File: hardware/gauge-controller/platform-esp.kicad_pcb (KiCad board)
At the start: 4 copper layers, 50 x 49.6 mm, 107 parts, among them J1 Conn_ARM_JTAG_SWD_10, J3 PWR_CAN, J4 USB4120-03-C_REVA, J6 TC2030-IDC, SW1 SW_Push, SW2 SW_Push, U1 W25Q128JVS, U2 ESP-PSRAM32, U3 ESP32-S3R2, U4 AP64200Q, U5 LTC2875-DD, Y1 40MHZ

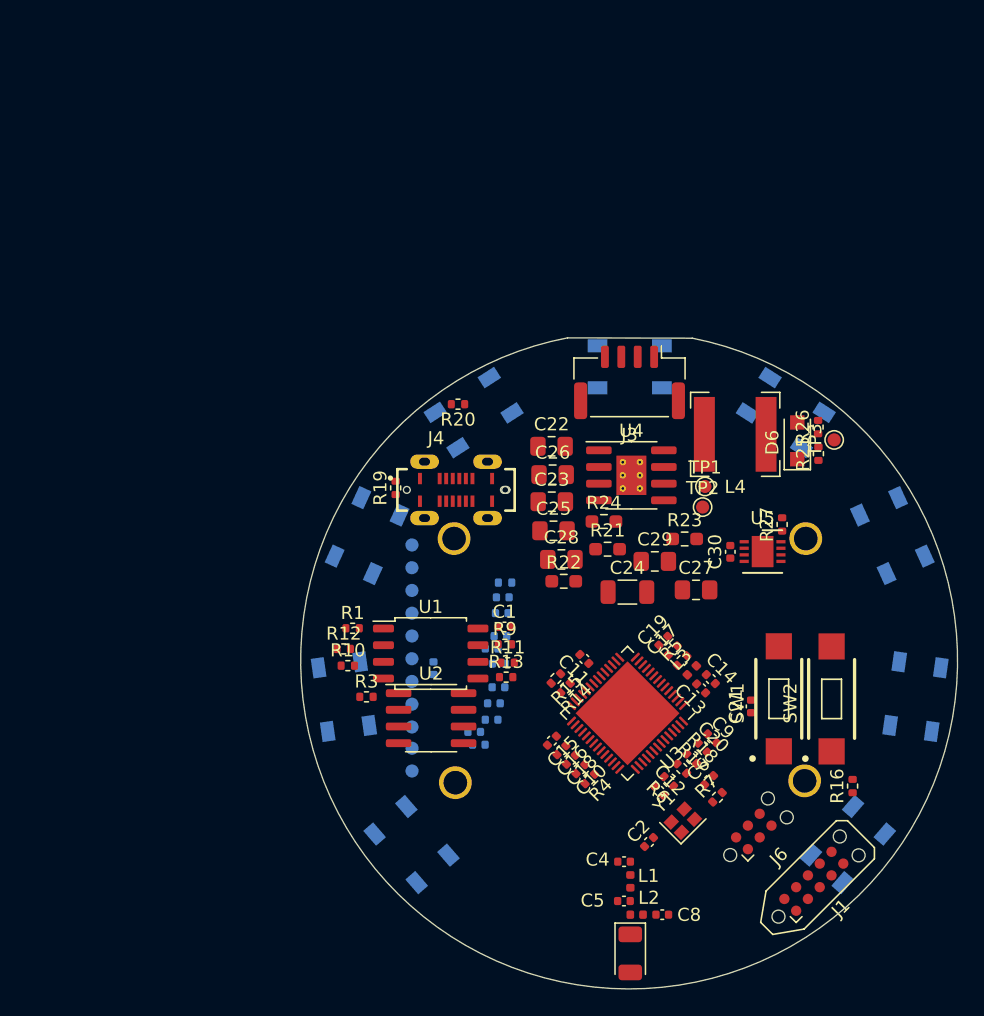
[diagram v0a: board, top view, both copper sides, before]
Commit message: Multi gauge pcb design
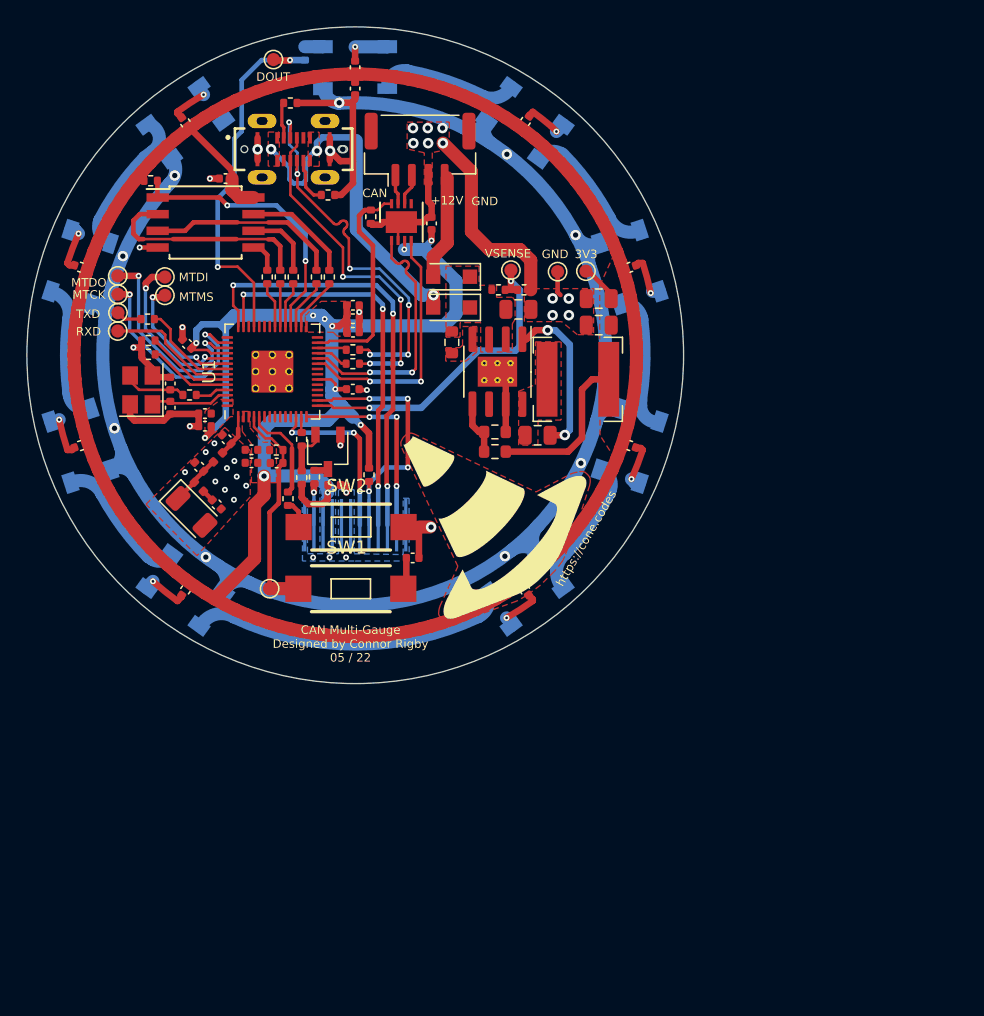
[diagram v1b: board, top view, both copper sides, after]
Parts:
- removed C23: 10uf, Capacitor_SMD:C_0805_2012Metric_Pad1.18x1.45mm_HandSolder
- removed C24: 5.6nf, Capacitor_SMD:C_1206_3216Metric
- removed C25: 0.1uf, Capacitor_SMD:C_0805_2012Metric_Pad1.18x1.45mm_HandSolder
- removed C26, C27: DNP, Capacitor_SMD:C_0805_2012Metric_Pad1.18x1.45mm_HandSolder
- removed C39, C40, C41, C42: 1uF, Capacitor_SMD:C_0402_1005Metric
- removed J3: PWR_CAN, Connector_JST:JST_GH_BM04B-GHS-TBT_1x04-1MP_P1.25mm_Vertical
- removed J6: TC2030-IDC, Connector:Tag-Connect_TC2030-IDC-NL_2x03_P1.27mm_Vertical
- removed L4: 6.8uh, Inductor_SMD:L_Bourns-SRN6028
- removed R29: 0, Resistor_SMD:R_0402_1005Metric
- removed REF**: 1.28-lcd, Module_Waveshare:1.28-lcd
- removed TP12: BL, TestPoint:TestPoint_Pad_D1.0mm
- removed TP13: VDD3V3, TestPoint:TestPoint_Pad_D1.0mm
- removed TP14: GND, TestPoint:TestPoint_Pad_D1.0mm
- removed U4: AP64200Q, Package_SO:SOIC-8-1EP_3.9x4.9mm_P1.27mm_EP2.29x3mm_ThermalVias
- added C3: C_Small, Capacitor_SMD:C_0402_1005Metric, F.Cu at (36.9, 47.0)
- added C31: 1uF, Capacitor_SMD:C_0402_1005Metric, F.Cu at (59.7, 22.7)
- added C7: 1uF, Capacitor_SMD:C_0402_1005Metric, F.Cu at (38.8, 47.8)
- added D7: WS2812B, WS2815B:LED_WS2812B_PLCC4_5.0x5.0mm_P3.2mm, B.Cu at (33.8, 22.9)
- added G***: LOGO, logos:cone, F.Cu at (55.9, 52.2)
- added J2: PWR_CAN, Connector_JST:JST_GH_BM04B-GHS-TBT_1x04-1MP_P1.25mm_Vertical, F.Cu at (51.7, 24.9)
- added Q1: Q_NPN_EBC, Package_TO_SOT_SMD:TSOT-23, F.Cu at (44.7, 47.9)
- added R2: 0, Resistor_SMD:R_0402_1005Metric, F.Cu at (34.1, 43.6)
- added R8: 100k, Resistor_SMD:R_0402_1005Metric, F.Cu at (31.2, 27.3)
- C1, C12, C18, C30: value 0.1uF -> 1uF
- C10: value 1uF -> 10uF; footprint Capacitor_SMD:C_0402_1005Metric -> Capacitor_SMD:C_0805_2012Metric
- C13, C2: value C_Small -> 10uF
- C14: value 0.1uF -> C_Small
- C15: value 1uF -> C_Small
- C16, C19: value 10uF -> 0.1uF
- C17: value 1uF -> 0.1uF
- C20: value 1uF -> 0.1uF; footprint Capacitor_SMD:C_0402_1005Metric -> Capacitor_SMD:C_0805_2012Metric
- C21: value 1uF -> 22uF; footprint Capacitor_SMD:C_0402_1005Metric -> Capacitor_SMD:C_0805_2012Metric
- C22: value 10uf -> 22uF; footprint Capacitor_SMD:C_0805_2012Metric_Pad1.18x1.45mm_HandSolder -> Capacitor_SMD:C_0805_2012Metric
- C28: value DNP -> 1uF; footprint Capacitor_SMD:C_0805_2012Metric_Pad1.18x1.45mm_HandSolder -> Capacitor_SMD:C_0402_1005Metric
- C29: value DNP -> 10uF; footprint Capacitor_SMD:C_0805_2012Metric_Pad1.18x1.45mm_HandSolder -> Capacitor_SMD:C_0402_1005Metric
- C32: value 10uF -> 1uF; moved to F.Cu
- C33, C34, C35, C36, C37, C38, TP5: moved to F.Cu
- C6, C8: value C_Small -> 0.1uF
- D1, D11: value WS2812B -> D_Small; footprint LED_SMD:LED_WS2812B_PLCC4_5.0x5.0mm_P3.2mm -> Diode_SMD:D_SOD-123F; moved to F.Cu
- D10, D2, D3, D4, D5, D8, D9: footprint LED_SMD:LED_WS2812B_PLCC4_5.0x5.0mm_P3.2mm -> WS2815B:LED_WS2812B_PLCC4_5.0x5.0mm_P3.2mm
- D6: value D_Small -> WS2812B; footprint Diode_SMD:D_SOD-123F -> WS2815B:LED_WS2812B_PLCC4_5.0x5.0mm_P3.2mm; moved to B.Cu
- J1: value Conn_ARM_JTAG_SWD_10 -> USB4120-03-C_REVA; footprint Connector:Tag-Connect_TC2050-IDC-NL_2x05_P1.27mm_Vertical -> ConeCodes:GCT_USB4120-03-C_REVA
- J4: value USB4120-03-C_REVA -> Conn_01x12; footprint Connector_GCT_USB:GCT_USB4120-03-C_REVA -> ConeCodes:GC9A01_disp; moved to B.Cu
- L3: value 0H -> 6.8uh; footprint Inductor_SMD:L_0402_1005Metric -> Inductor_SMD:L_Bourns-SRN6028
- R1: value 100k -> 10k
- R12, R13, R15: value 0 -> 10k
- R14: value 0 -> 36k
- R19: value 51k -> 100k; footprint Resistor_SMD:R_0402_1005Metric -> Resistor_SMD:R_0603_1608Metric
- R20: value 51k -> 31k6; footprint Resistor_SMD:R_0402_1005Metric -> Resistor_SMD:R_0603_1608Metric
- R21: value 200k -> 10k2; footprint Resistor_SMD:R_0603_1608Metric_Pad0.98x0.95mm_HandSolder -> Resistor_SMD:R_0603_1608Metric
- R22: value 14k -> 10k; footprint Resistor_SMD:R_0603_1608Metric_Pad0.98x0.95mm_HandSolder -> Resistor_SMD:R_0402_1005Metric
- R23: value 52.3k -> 51k; footprint Resistor_SMD:R_0603_1608Metric_Pad0.98x0.95mm_HandSolder -> Resistor_SMD:R_0402_1005Metric
- R24: value 10k -> 51k; footprint Resistor_SMD:R_0603_1608Metric_Pad0.98x0.95mm_HandSolder -> Resistor_SMD:R_0402_1005Metric
- R25: value 36k -> 0; moved to B.Cu
- R26: value 10k -> 10R
- R27: value 10k -> 100k
- R3: value 100k -> 499
- R4: value 442k -> 0
- R5: value 10k -> 0
- R6: value 499 -> 0
- SW1, SW2: footprint SW_RS-032G05A3-SMRT:SW_RS-032G05A3-SMRT -> ConeCodes:SW_RS-032G05A3-SMRT
- TP1: value 3V3OUT -> CHIP_PU
- TP10: value DC -> 3V3OUT; moved to F.Cu
- TP11: value RST -> 3V3OUT; moved to F.Cu
- TP2: value 3V3OUT -> VBAT_SENSE
- TP3: value VBAT_SENSE -> MTCK
- TP4: value CHIP_PU -> MTMS; moved to F.Cu
- TP6: value FSPID -> MTDO; moved to F.Cu
- TP7: value FSPICS1 -> MTDI; moved to F.Cu
- TP8: value FSPIQ -> TXD; moved to F.Cu
- TP9: value FSPICLK -> RXD; moved to F.Cu
- U1: value W25Q128JVS -> ESP32-S3R2; footprint Package_SO:SOIC-8_5.23x5.23mm_P1.27mm -> ConeCodes:QFN-56
- U2: value ESP-PSRAM32 -> LTC2875-DD; footprint Package_SO:SOIC-8_3.9x4.9mm_P1.27mm -> Package_DFN_QFN:DFN-8-1EP_3x3mm_P0.5mm_EP1.66x2.38mm
- U3: value ESP32-S3R2 -> W25Q128JVS; footprint Package_DFN_QFN:QFN-56-1EP_7x7mm_P0.4mm_EP5.6x5.6mm -> Package_SO:SOIC-8W_5.3x5.3mm_P1.27mm
- U5: value LTC2875-DD -> ADP2303ARDZ-3.3; footprint Package_DFN_QFN:DFN-8-1EP_3x3mm_P0.5mm_EP1.66x2.38mm -> Package_SO:SOIC-8-1EP_3.9x4.9mm_P1.27mm_EP2.29x3mm_ThermalVias
- Y1: footprint Crystal:Crystal_SMD_2016-4Pin_2.0x1.6mm -> Crystal:Crystal_SMD_3225-4Pin_3.2x2.5mm
- moved J1 68.4 mm to (42.0, 24.9), turned to 0 degrees
- moved TP3 55.7 mm to (28.7, 35.9)
- moved Y1 52.7 mm to (30.4, 43.2), turned to 90 degrees
- moved TP5 51.9 mm to (40.5, 18.0), turned to 0 degrees
- moved R17 51.5 mm to (31.0, 40.5), turned to 180 degrees
- moved C38 50.1 mm to (33.8, 22.9), turned to 126 degrees
- moved R7 50.1 mm to (43.8, 34.6), turned to -90 degrees
- moved C9 50.0 mm to (33.9, 39.7), turned to 135 degrees
- moved R25 49.6 mm to (42.9, 17.6)
- moved C17 49.5 mm to (36.9, 27.1), turned to 180 degrees
- moved U3 49.3 mm to (35.3, 30.4), turned to 0 degrees
- moved AE1 47.4 mm to (34.3, 52.5), turned to -45 degrees
- moved C30 46.7 mm to (46.7, 18.6)
- moved L2 46.7 mm to (34.8, 50.6), turned to -45 degrees
- moved C8 46.5 mm to (46.6, 43.1), turned to 0 degrees
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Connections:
- C10 pad 1: /SPICLK_P -> GND
- C10 pad 2: GND -> /VIN
- C11 pad 1: /VDDRTC -> +3V3
- C12 pad 1: /VDDCPU -> +3V3
- C13 pad 1: GND -> +3V3
- C13 pad 2: /VDD3V3 -> GND
- C14 pad 1: +3V3 -> /XTAL_P
- C15 pad 1: +3V3 -> /XTAL_N
- C18 pad 1: +3V3 -> /CHIP_PU_BOOTSTRAP
- C19 pad 1: +3V3 -> /CHIP_PU
- C19 pad 2: GND -> +3V3
- C2 pad 1: /XTAL_P -> +3V3
- C20 pad 1: +3V3 -> /BST
- C20 pad 2: GND -> /SW
- C21 pad 1: Net-(C21-Pad1) -> +3V3
- C22 pad 1: GND -> +3V3
- C22 pad 2: /VIN -> GND
- C30 pad 2: GND -> Net-(C30-Pad2)
- C32 pad 2: GND -> Net-(C32-Pad2)
- C4 pad 2: /LNA_IN -> /RF_ANT
- C5 pad 2: /RF_ANT -> Net-(C5-Pad2)
- C6 pad 1: /XTAL_N -> +3V3
- C8 pad 1: GND -> +3V3
- C8 pad 2: Net-(C8-Pad2) -> GND
- D1 pad 1: Net-(C33-Pad2) -> /VIN
- D1 pad 2: Net-(D1-Pad2) -> /EXT_VIN
- D10 pad 1: Net-(C40-Pad2) -> Net-(C37-Pad2)
- D11 pad 1: Net-(C41-Pad2) -> /VIN
- D11 pad 2: unconnected-(D11-Pad2) -> /USB_VBUS
- D2 pad 1: Net-(C34-Pad2) -> Net-(C30-Pad2)
- D2 pad 4: Net-(D1-Pad2) -> Net-(D2-Pad4)
- D3 pad 1: Net-(C35-Pad2) -> Net-(C31-Pad2)
- D4 pad 1: Net-(C36-Pad2) -> Net-(C32-Pad2)
- D5 pad 1: Net-(C37-Pad2) -> Net-(C33-Pad2)
- D6 pad 1: /VIN -> Net-(C34-Pad2)
- D6 pad 2: /EXT_VIN -> Net-(D6-Pad2)
- D8 pad 1: Net-(C38-Pad2) -> Net-(C35-Pad2)
- D8 pad 4: Net-(D5-Pad2) -> Net-(D6-Pad2)
- D9 pad 1: Net-(C39-Pad2) -> Net-(C36-Pad2)
- L2 pad 2: Net-(C8-Pad2) -> Net-(C5-Pad2)
- L3 pad 1: /VDD3V3 -> /SW
- R1 pad 1: +3V3 -> /CHIP_PU
- R1 pad 2: /SPICS0 -> +3V3
- R10 pad 1: /SPIWP -> /SPIQ
- R10 pad 2: Net-(R10-Pad2) -> /MCU_SPIQ
- R11 pad 1: /SPICLK -> /SPID
- R11 pad 2: Net-(R11-Pad2) -> /MCU_SPID
- R12 pad 1: /SPIQ -> /CAN_EN
- R12 pad 2: Net-(R12-Pad2) -> GND
- R13 pad 1: /SPID -> /GPIO0
- R13 pad 2: Net-(R13-Pad2) -> /GPIO0_BOOTSTRAP
- R14 pad 1: /GPIO_USB_D_N -> /VIN
- R14 pad 2: /USB_D_N -> /GPIO10
- R15 pad 1: /GPIO_USB_D_P -> /GPIO45
- R15 pad 2: /USB_D_P -> GND
- R16 pad 1: /GPIO0 -> /GPIO10
- R16 pad 2: /GPIO0_BOOTSTRAP -> GND
- R17 pad 1: /GPIO45 -> /GPIO46
- R18 pad 1: /GPIO46 -> /BL
- R18 pad 2: GND -> /LCD_BL_DIV
- R19 pad 1: /CC2 -> /VIN
- R19 pad 2: GND -> /PGOOD
- R20 pad 1: /CC1 -> +3V3
- R20 pad 2: GND -> /FB
- R21 pad 1: Net-(R21-Pad1) -> /FB
- R22 pad 1: Net-(C26-Pad1) -> /LCD_BL_DIV
- R22 pad 2: Net-(C24-Pad1) -> +3V3
- R23 pad 1: +3V3 -> /CC1
- R23 pad 2: Net-(C27-Pad2) -> GND
- R24 pad 1: Net-(C27-Pad2) -> /CC2
- R25 pad 1: /VIN -> /GPIO34
- R25 pad 2: /GPIO2 -> Net-(D2-Pad4)
- R26 pad 1: /GPIO2 -> /LCD_LEDK
- R26 pad 2: GND -> /Q_LEDK
- R27 pad 1: /CAN_EN -> +3V3
- R27 pad 2: GND -> /FSPICS0
- R3 pad 1: /SPICS1 -> /U0TXD
- R3 pad 2: +3V3 -> /MCU_U0TXD
- R4 pad 1: /SPICLK_P -> /GPIO_USB_D_N
- R4 pad 2: GND -> /USB_D_N
- R5 pad 1: /CHIP_PU -> /GPIO_USB_D_P
- R5 pad 2: +3V3 -> /USB_D_P
- R6 pad 1: /U0TXD -> /SPIHD
- R6 pad 2: Net-(R6-Pad2) -> /MCU_SPIHD
- R7 pad 1: /XTAL_N -> /SPIWP
- R7 pad 2: Net-(R7-Pad2) -> /MCU_SPIWP
- R9 pad 1: /SPIHD -> /SPICLK
- R9 pad 2: Net-(R9-Pad2) -> /MCU_SPICLK
- SW1 pad 2: Net-(C21-Pad1) -> /CHIP_PU_BOOTSTRAP
- TP1 pad 1: GND -> /CHIP_PU
- TP10 pad 1: /DC -> GND
- TP11 pad 1: /GPIO6 -> +3V3
- TP2 pad 1: +3V3 -> /GPIO10
- TP3 pad 1: /GPIO2 -> /MTCK
- TP4 pad 1: /CHIP_PU -> /MTMS
- TP5 pad 1: /GPIO14 -> /GPIO34
- TP6 pad 1: /FSPID -> /MTDO
- TP7 pad 1: /FSPICS1 -> /MTDI
- TP8 pad 1: /FSPIQ -> /U0TXD
- TP9 pad 1: /FSPICLK -> /U0RXD
- U1 pad 1: /SPICS0 -> /LNA_IN
- U1 pad 2: /SPIQ -> +3V3
- U1 pad 3: /SPIWP -> +3V3
- U1 pad 4: GND -> /CHIP_PU
- U1 pad 5: /SPID -> /GPIO0
- U1 pad 6: /SPICLK -> /GPIO1
- U1 pad 7: /SPIHD -> /GPIO2
- U1 pad 8: +3V3 -> /GPIO3
- U2 pad 1: /SPICS1 -> /CAN_P
- U2 pad 2: /SPID -> GND
- U2 pad 3: /SPIWP -> +3V3
- U2 pad 4: GND -> /CAN_N
- U2 pad 5: /SPIQ -> unconnected-(U2-Pad5)
- U2 pad 6: /SPICLK -> /CAN_DRV_N
- U2 pad 7: /SPIHD -> /CAN_DRV_P
- U2 pad 8: +3V3 -> /CAN_EN
- U3 pad 1: /LNA_IN -> /MCU_SPICS0
- U3 pad 2: /VDD3V3 -> /SPIQ
- U3 pad 3: /VDD3V3 -> /SPIWP
- U3 pad 4: /CHIP_PU -> GND
- U3 pad 5: /GPIO0 -> /SPID
- U3 pad 6: /GPIO1 -> /SPICLK
- U3 pad 7: /GPIO2 -> /SPIHD
- U3 pad 8: /GPIO3 -> +3V3
- U5 pad 1: /CAN_P -> /BST
- U5 pad 2: GND -> /VIN
- U5 pad 3: +3V3 -> /VIN
- U5 pad 4: /CAN_N -> /PGOOD
- U5 pad 5: unconnected-(U5-Pad5) -> /FB
- U5 pad 6: /CAN_DRV_N -> unconnected-(U5-Pad6)
- U5 pad 7: /CAN_DRV_P -> GND
- U5 pad 8: /CAN_EN -> /SW
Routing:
- net +3V3: track 0.00 -> 256.2 mm, vias 0 -> 11
- net GND: track 0.00 -> 183.9 mm, vias 0 -> 44
- net /FSPIQ: track 0.00 -> 33.3 mm, vias 0 -> 3
- net /FSPICLK: track 0.00 -> 30.3 mm, vias 0 -> 3
- net /USB_D_P: track 0.00 -> 30.1 mm, vias 0 -> 6
- net /GPIO34: track 0.00 -> 28.3 mm, vias 0 -> 2
- net /USB_VBUS: track 0.00 -> 26.8 mm, vias 0 -> 3
- net /USB_D_N: track 0.00 -> 25.7 mm, vias 0 -> 4
- net /GPIO10: track 0.00 -> 25.2 mm, vias 0 -> 2
- net Net-(D6-Pad2): track 0.00 -> 24.0 mm
- net /MCU_SPICS0: track 0.00 -> 21.2 mm, vias 0 -> 2
- net /FSPICS0: track 0.00 -> 19.7 mm, vias 0 -> 4
- net /CAN_N: track 0.00 -> 19.5 mm, vias 0 -> 2
- net /CAN_P: track 0.00 -> 19.4 mm, vias 0 -> 2
- net /MTCK: track 0.00 -> 16.9 mm, vias 0 -> 2
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- added copper zone on F.Cu, net (none)
- added copper zone on B.Cu, net +3V3
- added copper zone on F.Cu, net +3V3
- added copper zone on F.Cu, net /PGOOD
- added copper zone on F.Cu, net /SW
- added copper zone on F.Cu, net /USB_VBUS
- added copper zone on F.Cu, net /VIN
- added copper zone on B.Cu, net GND
- added copper zone on F.Cu, net GND
- added copper zone on In1.Cu, net GND
- added copper zone on In2.Cu, net GND
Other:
- board size 50 x 49.6 mm -> 50 x 50 mm
- board text added: "+12V"
- board text added: "3V3"
- board text added: "CAN"
- board text added: "CAN Multi-Gauge"
- board text added: "DOUT"
- board text added: "Designed by Connor Rigby 05 / 22"
- board text added: "GND"
- board text added: "MTCK"
- board text added: "MTDI"
- board text added: "MTDO"
- board text added: "MTMS"
- board text added: "RXD"
- board text added: "TXD"
- board text added: "VSENSE"
- board text added: "https://cone.codes"

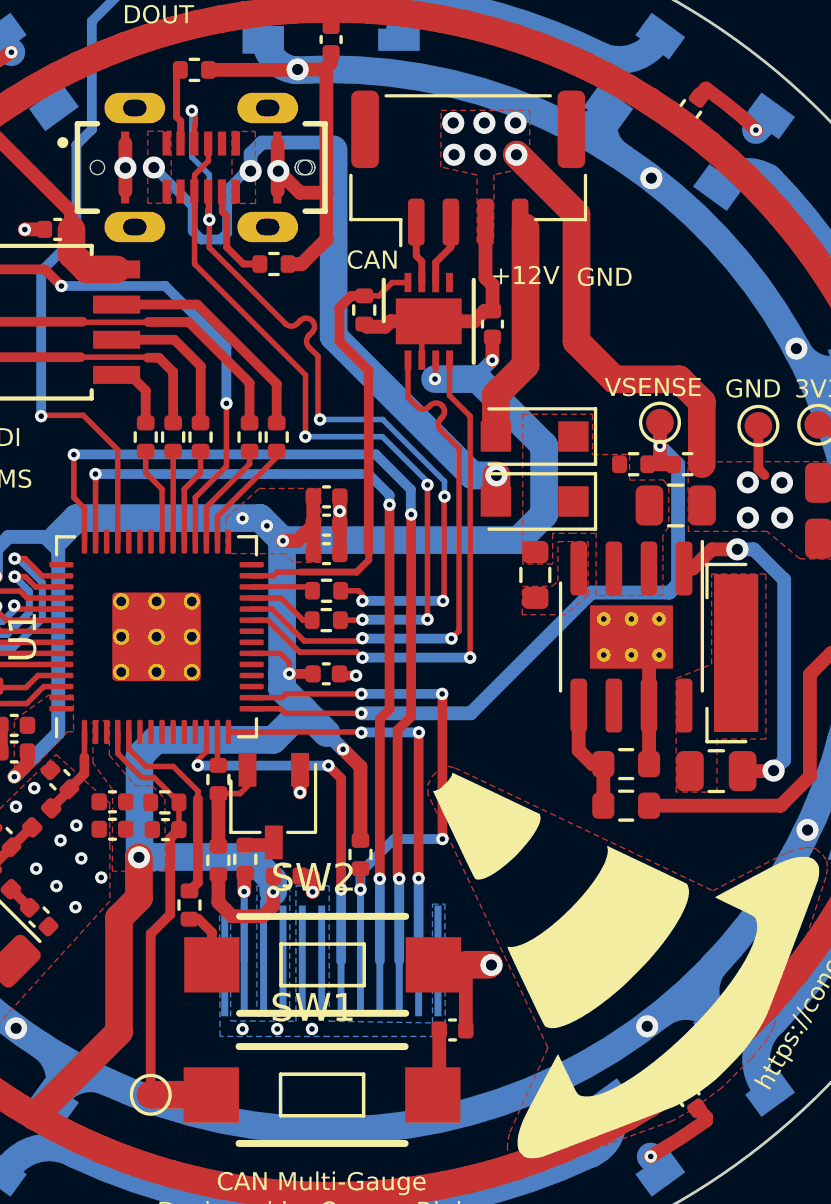
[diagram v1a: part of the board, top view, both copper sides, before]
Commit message: Update PCBs to share the same components
* 3x flash memory
* CAN transciever
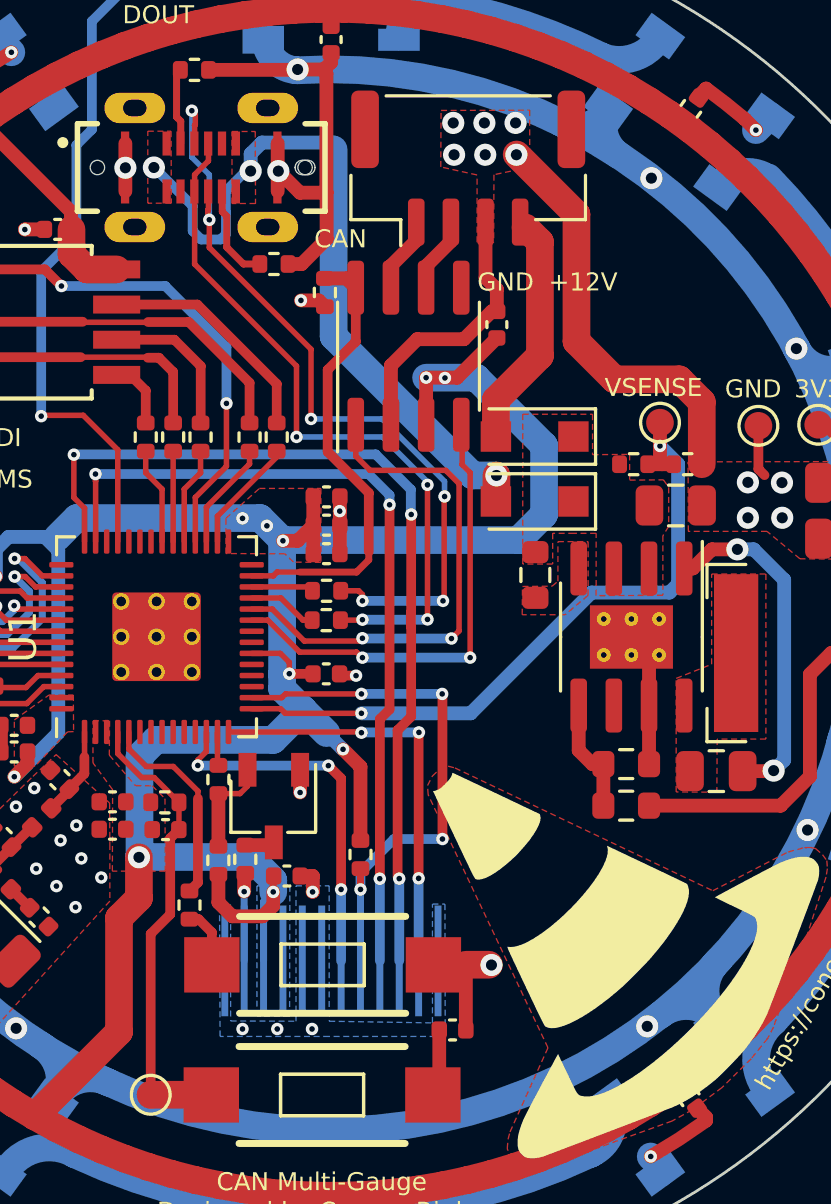
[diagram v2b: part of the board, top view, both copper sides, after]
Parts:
- U2: value LTC2875-DD -> SN65HVD230; footprint Package_DFN_QFN:DFN-8-1EP_3x3mm_P0.5mm_EP1.66x2.38mm -> Package_SO:SOIC-8_3.9x4.9mm_P1.27mm
- moved R12 1.55 mm to (46.5, 29.4)
- moved U2 1.46 mm to (49.5, 31.7)
- moved C16 0.16 mm to (52.7, 30.5)
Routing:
- net +3V3: track 256.2 -> 259.3 mm
- net /CAN_N: track 19.5 -> 17.0 mm
- net GND: track 183.9 -> 185.6 mm, vias 44 -> 45
- net /USB_D_P: track 30.1 -> 29.3 mm
- net /CAN_P: track 19.4 -> 18.7 mm
